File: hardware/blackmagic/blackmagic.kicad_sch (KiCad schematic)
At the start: 42 parts, among them U1 STM32F411CEUx, U2 USBLC6-2P6, U3 AP2112K-3.3TRG1, X1 32.768kHz crystal, X2 25Mhz crystal

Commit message: Add all indication LEDs to the schema
Move LEDs from PC13-PC15 to PB13-PB15 correspondingly. According to the datasheet, "PC13, PC14 and PC15 are supplied through the power switch" and "These I/Os must not be used as a current source (e.g. to drive an LED)". No idea why are they used for LEDs in the BMP firmware. Those LEDs are also seemingly don't work on my HITL carrier board.
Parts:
- removed LED3: 17-21SUYC/TR8, easyeda2kicad:LED0805-R-RD, symbol easyeda2kicad:17-21SUYC_TR8
- added LED2: Yellow, easyeda2kicad:LED0805-R-RD, symbol easyeda2kicad:17-21SUYC_TR8
- added LED3: White, easyeda2kicad:LED0603-R-RD_WHITE, symbol easyeda2kicad:LED White
- added LED5: Green, easyeda2kicad:LED0805-R-RD, symbol easyeda2kicad:0805G(Green)
- added R8, R9: 330R, Resistor_SMD:R_0603_1608Metric, symbol Ostranna:100R Resistor
- LED1: renamed from LED2; value 0805G (Green) -> Green
- LED4: value KT-0603R -> Red
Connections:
- net +3V3: now also R9.2
- net GND: now also LED2.2 (-), LED3.2 (K), LED5.2 (K)
- net LED_BOOTLOADER: now also U1.28 (PB15)
- net LED_ERROR: now also U1.27 (PB14)
- net at R5.1: now also LED3.1 (A)
- net PWR_BR: now reaches U1.11 (PA1)
- net LED_IDLE: now reaches U1.26 (PB13)
- net LED_IDLE: now also R8.2
- new net: LED2.1 (+), R8.1
- new net: LED5.1 (A), R9.1
- no-connect marks 34 -> 30
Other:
- note added: "TODO: Add user butttons? Why are they needed?"
- note removed: "TODO: Add "always on when powered" LED"
- note removed: "TODO: Figure out good pins for them"
- moved on the sheet: C15, C16, C17, C18, JP1, LED1, R3, R4, R5, R7, X1, X2

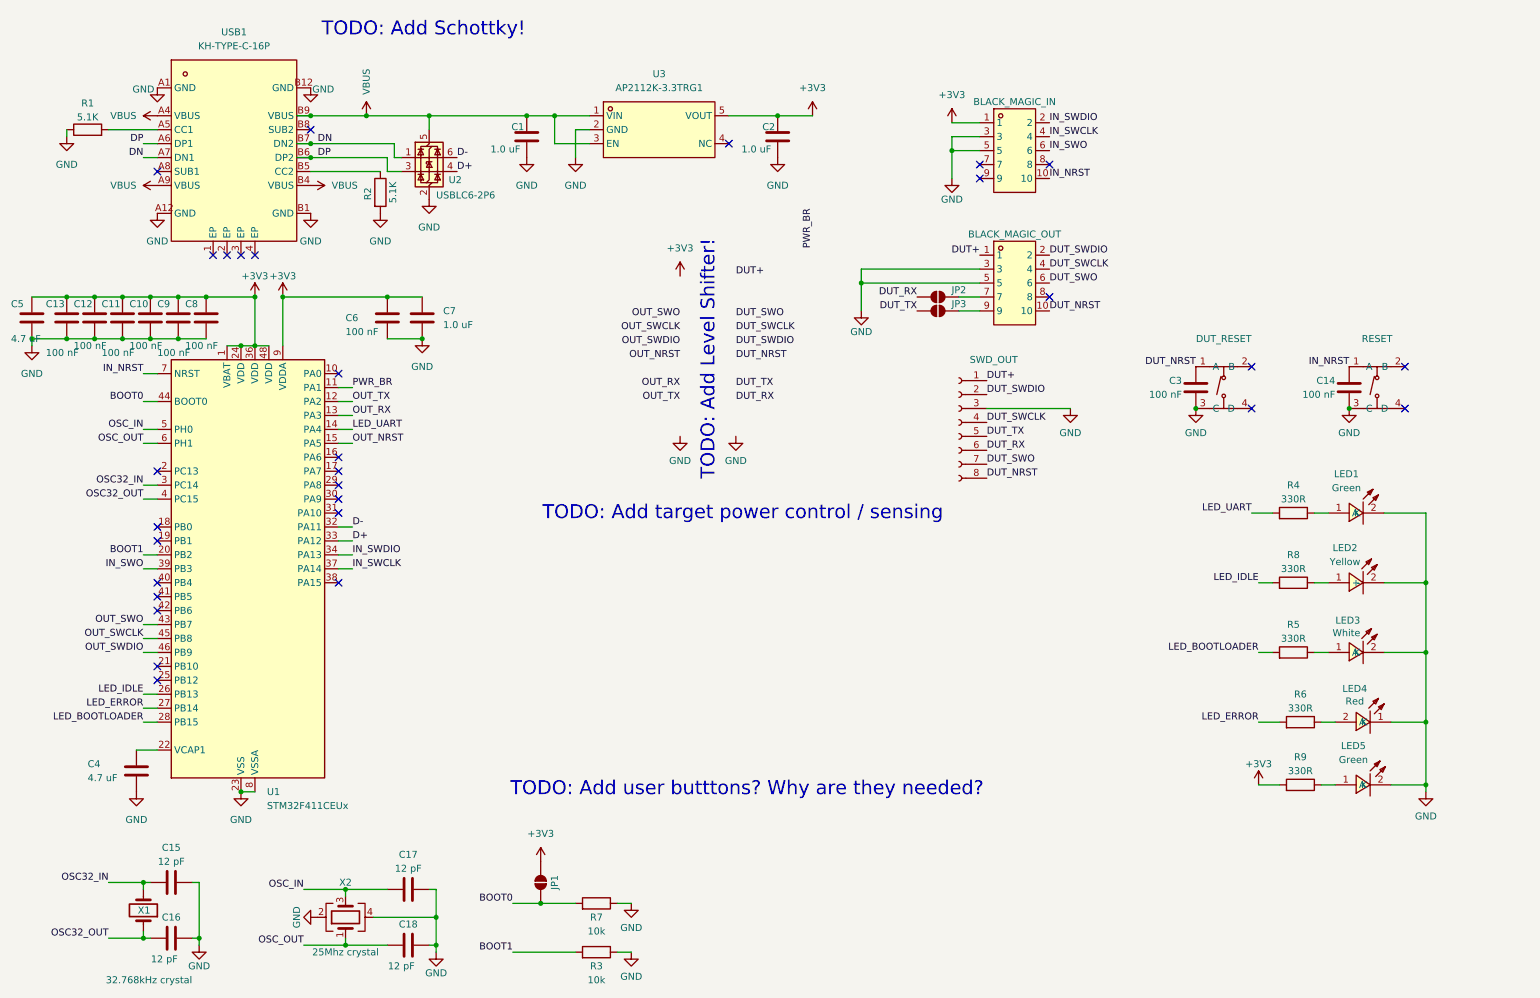
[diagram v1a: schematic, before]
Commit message: Finish with the blackmagic schematic
Now it's layout/routing time!
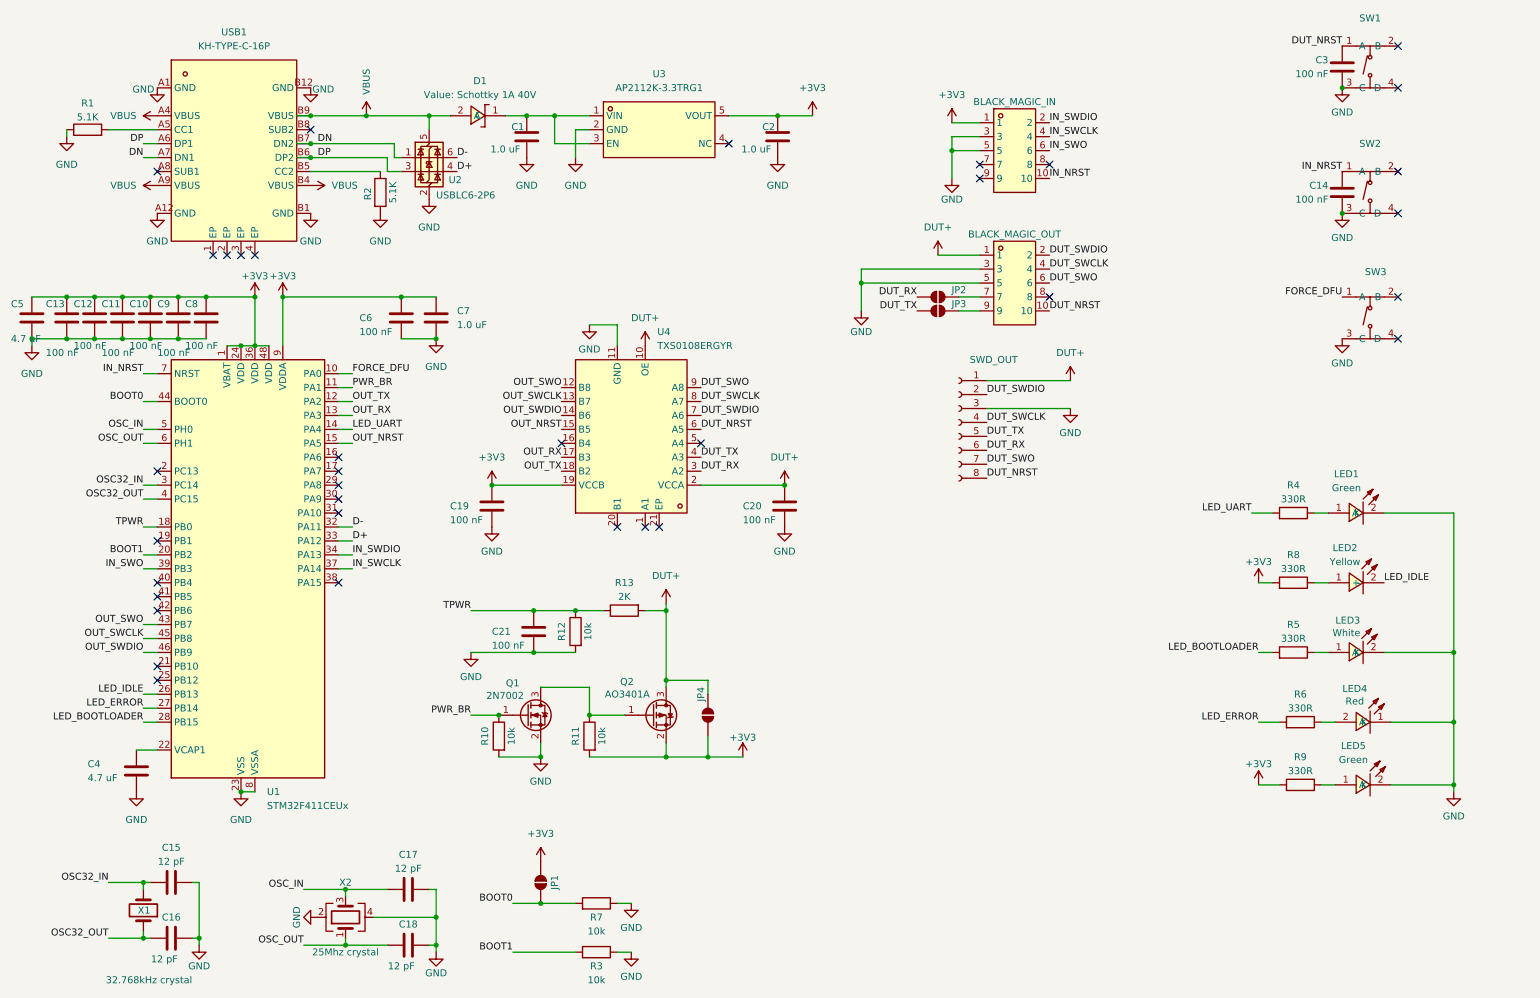
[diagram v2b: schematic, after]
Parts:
- added C19, C20, C21: 100 nF, Capacitor_SMD:C_0402_1005Metric, symbol Ostranna:100 nF
- added D1: Schottky 1A 40V, easyeda2kicad:SOD-323_L1.8-W1.3-LS2.5-RD, symbol easyeda2kicad:Schottky 1A 40V
- added JP4: SolderJumper_2_Open, Jumper:SolderJumper-2_P1.3mm_Open_RoundedPad1.0x1.5mm, symbol Jumper:SolderJumper_2_Open
- added Q1: 2N7002, Package_TO_SOT_SMD:SOT-23, symbol Ostranna:2N7002
- added Q2: AO3401A, Package_TO_SOT_SMD:SOT-23, symbol Ostranna:IRML6401
- added R10, R11, R12: 10k, Resistor_SMD:R_0402_1005Metric, symbol Ostranna:10k Resistor
- added R13: 2K, Resistor_SMD:R_0402_1005Metric, symbol Ostranna:10k Resistor
- added SW3: TS-1187A-B-A-B, easyeda2kicad:SW-SMD_4P-L5.1-W5.1-P3.70-LS6.5-TL-2, symbol easyeda2kicad:TS-1187A-B-A-B
- added U4: TXS0108ERGYR, easyeda2kicad:VQFN-20_L4.6-W3.6-P0.50-BL-EP, symbol easyeda2kicad:TXS0108ERGYR
- renumbered DUT_RESET to SW1, RESET to SW2
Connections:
- net +3V3: now also R8.2, C19.1, JP4.2 (B), Q2.2 (S), R11.1, U4.19 (VCCB)
- net DUT+: now also C20.1, JP4.1 (A), Q2.3 (D), R13.1, U4.10 (OE), U4.2 (VCCA)
- net DUT_NRST: now also U4.6 (A5)
- net DUT_RX: now also U4.3 (A2)
- net DUT_SWCLK: now also U4.8 (A7)
- net DUT_SWDIO: now also U4.7 (A6)
- net DUT_SWO: now also U4.9 (A8)
- net DUT_TX: now also U4.4 (A3)
- net GND: now also C19.2, C20.2, C21.2, Q1.2 (S), R10.1, R12.1, SW3.3 (C), U4.11 (GND); no longer LED2.2 (-)
- net LED_IDLE: now also LED2.2 (-); no longer R8.2
- net OUT_NRST: now also U4.15 (B5)
- net OUT_RX: now also U4.17 (B3)
- net OUT_SWCLK: now also U4.13 (B7)
- net OUT_SWDIO: now also U4.14 (B6)
- net OUT_SWO: now also U4.12 (B8)
- net OUT_TX: now also U4.18 (B2)
- net PWR_BR: now also Q1.1 (G), R10.2
- net VBUS: now also D1.2 (A); no longer C1.1, U3.1 (VIN), U3.3 (EN)
- net FORCE_DFU: now reaches U1.10 (PA0)
- net FORCE_DFU: now also SW3.1 (A)
- net TPWR: now reaches U1.18 (PB0)
- net TPWR: now also C21.1, R12.2, R13.2
- new net: C1.1, D1.1 (C), U3.1 (VIN), U3.3 (EN)
- new net: Q1.3 (D), Q2.1 (G), R11.2
- no-connect marks 30 -> 35
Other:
- note removed: "TODO: Add Level Shifter!"
- note removed: "TODO: Add Schottky!"
- note removed: "TODO: Add target power control / sensing"
- note removed: "TODO: Add user butttons? Why are they needed?"
- moved on the sheet: C14, C3, C6, C7, SW1, SW2

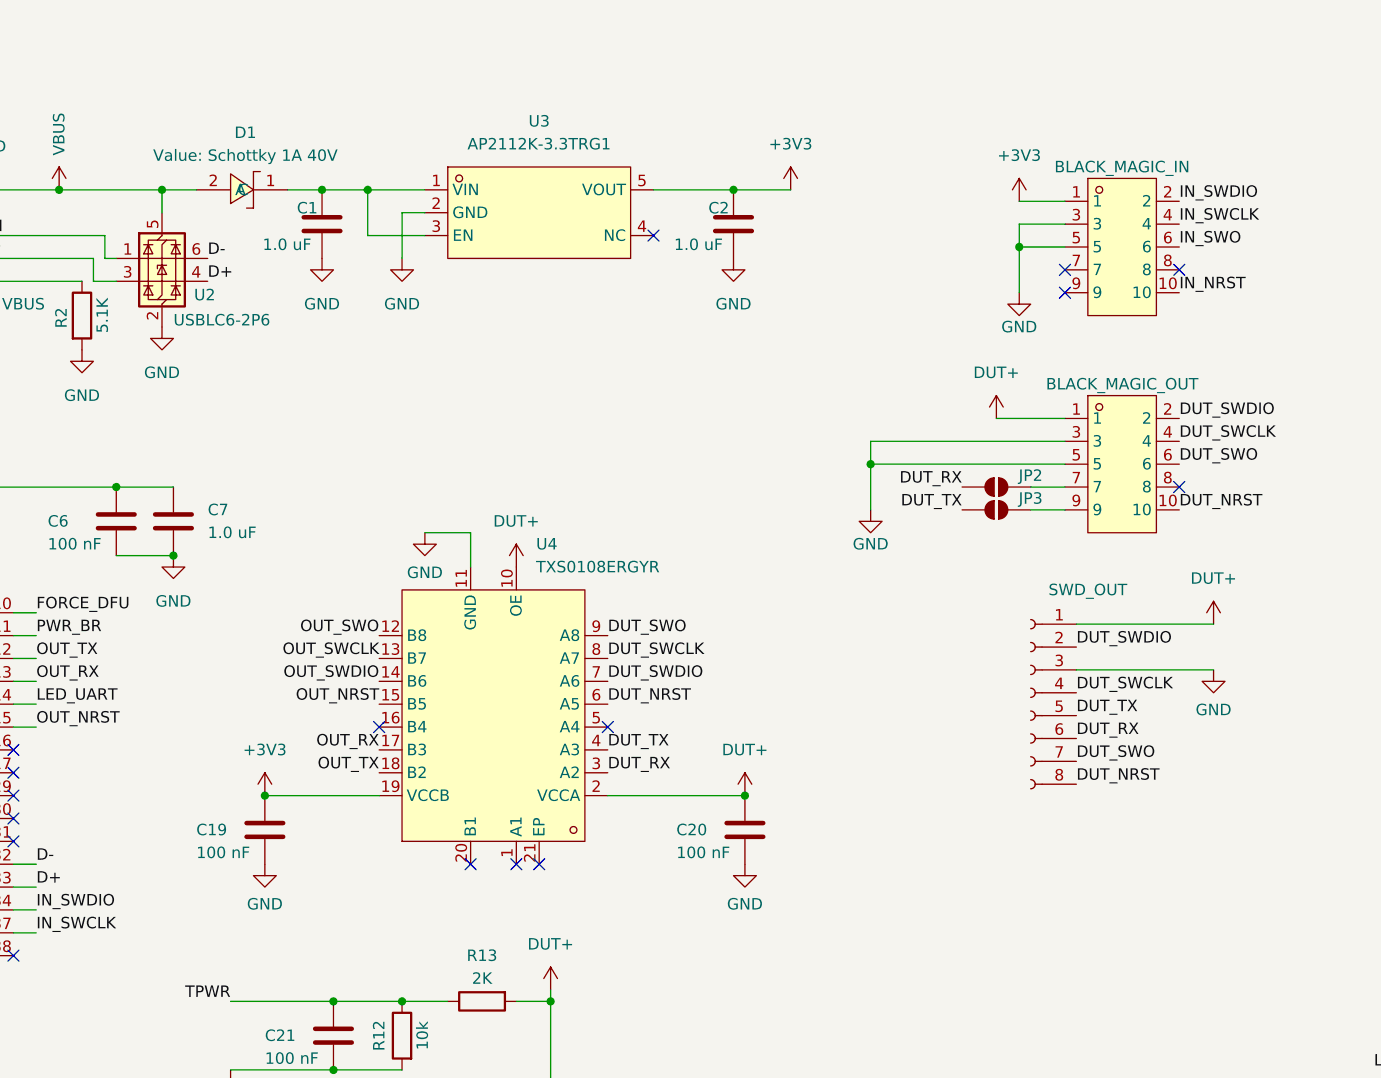
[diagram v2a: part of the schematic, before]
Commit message: Finish with the first pass of the routing
Still need to add some GND vias and clean things up
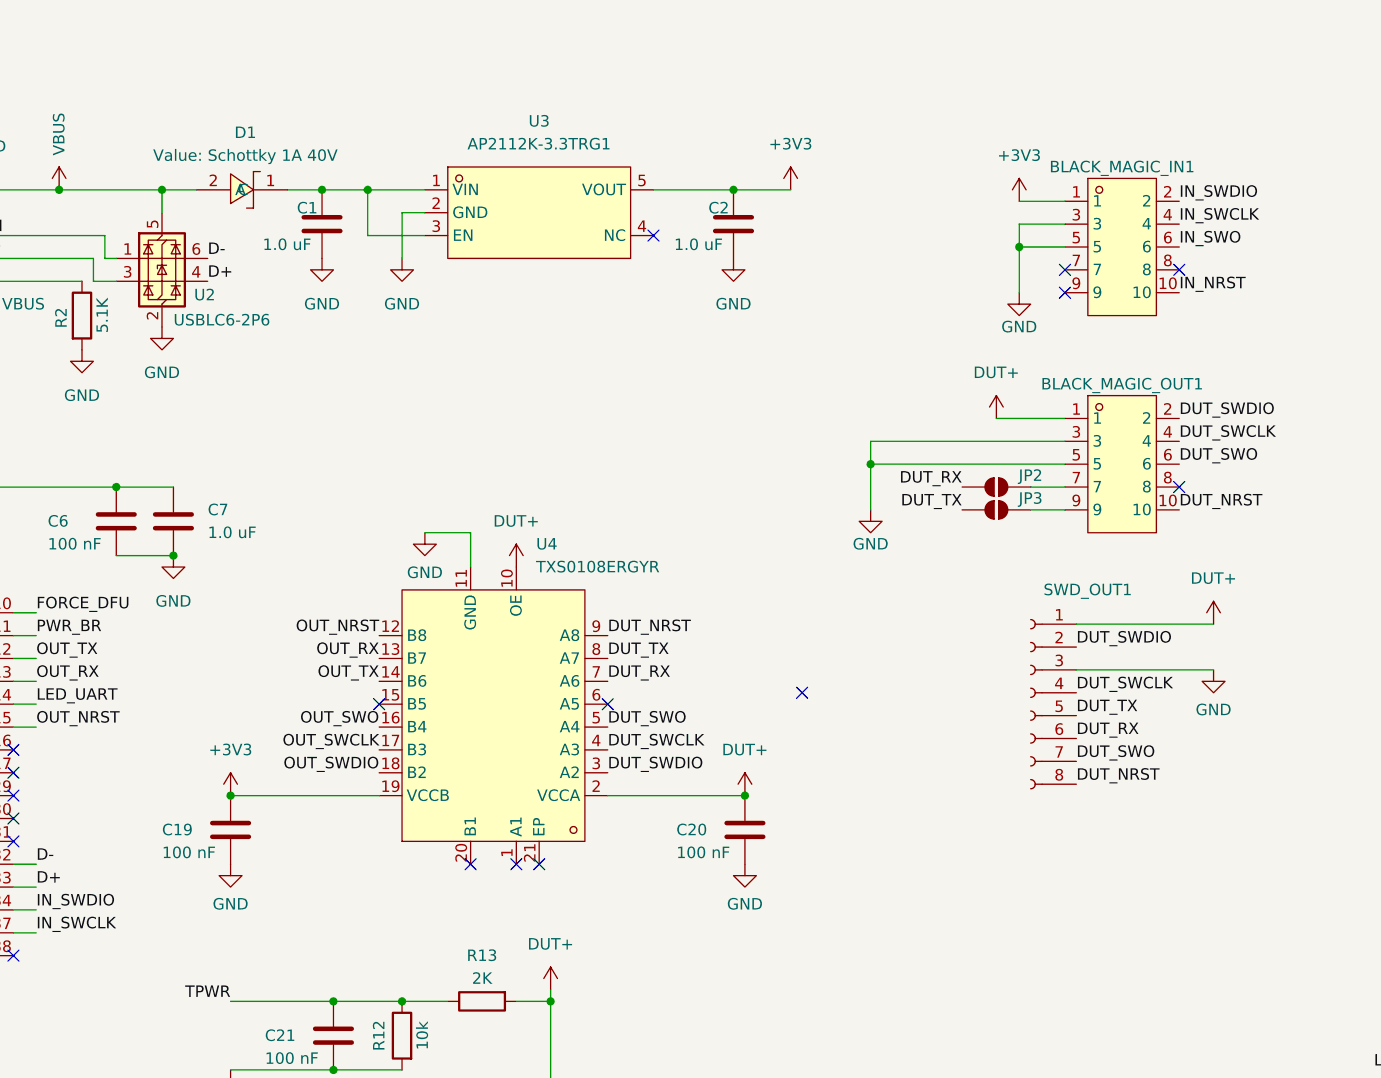
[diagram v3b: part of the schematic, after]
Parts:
- renumbered BLACK_MAGIC_IN to BLACK_MAGIC_IN1, BLACK_MAGIC_OUT to BLACK_MAGIC_OUT1, SWD_OUT to SWD_OUT1
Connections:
- net DUT_NRST: now also U4.9 (A8); no longer U4.6 (A5)
- net DUT_RX: now also U4.7 (A6); no longer U4.3 (A2)
- net DUT_SWCLK: now also U4.4 (A3); no longer U4.8 (A7)
- net DUT_SWDIO: now also U4.3 (A2); no longer U4.7 (A6)
- net DUT_SWO: now also U4.5 (A4); no longer U4.9 (A8)
- net DUT_TX: now also U4.8 (A7); no longer U4.4 (A3)
- net OUT_NRST: now also U4.12 (B8); no longer U4.15 (B5)
- net OUT_RX: now also U4.13 (B7); no longer U4.17 (B3)
- net OUT_SWCLK: now also U4.17 (B3); no longer U4.13 (B7)
- net OUT_SWDIO: now also U4.18 (B2); no longer U4.14 (B6)
- net OUT_SWO: now also U4.16 (B4); no longer U4.12 (B8)
- net OUT_TX: now also U4.14 (B6); no longer U4.18 (B2)
- no-connect marks 35 -> 36
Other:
- moved on the sheet: C19

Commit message: Finish blackmagic board and send it to production
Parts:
- added H1, H2, H3, H4: MountingHole, MountingHole:MountingHole_2.2mm_M2, symbol Mechanical:MountingHole
- BLACK_MAGIC_IN1, SWD_OUT1: now not fitted
- U1: footprint Package_DFN_QFN:QFN-48-1EP_7x7mm_P0.5mm_EP5.6x5.6mm -> easyeda2kicad:UFQFPN-48_L7.0-W7.0-P0.50-BL-EP; LCSC (none) -> C60420
- U2: footprint Package_TO_SOT_SMD:SOT-666 -> easyeda2kicad:SOT-666-6_L1.6-W1.2-P0.50-LS1.6-BR
